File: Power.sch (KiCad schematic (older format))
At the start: 39 parts, among them J10 AUX, J8 MCU_CURRENT, J9 RAM_CURRENT, U1 ATXMEGA128A1U-AU, U4 SN74AHC573PW, U6 TPS2110A, U7 LM3671MF

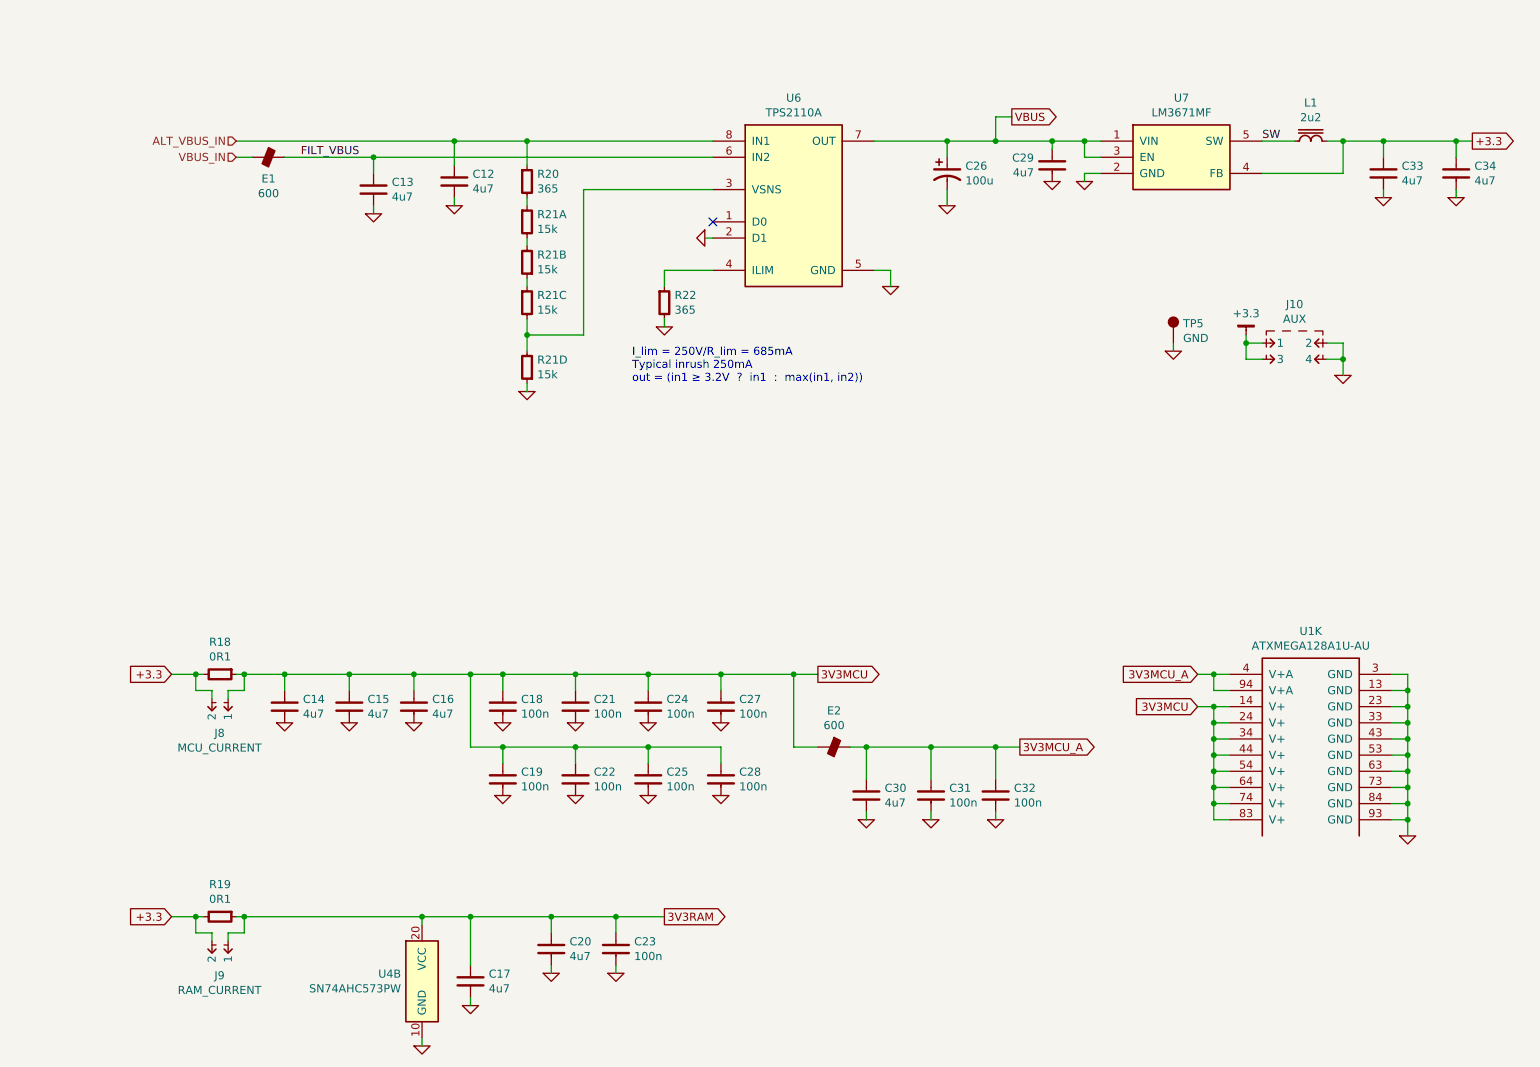
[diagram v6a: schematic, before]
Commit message: Remove extra resistor R20
With increase of R21 to 15k, it became insignificant - judged better
to remove it and push the power switching threshold a bit lower than
to add another BOM item to increase it.
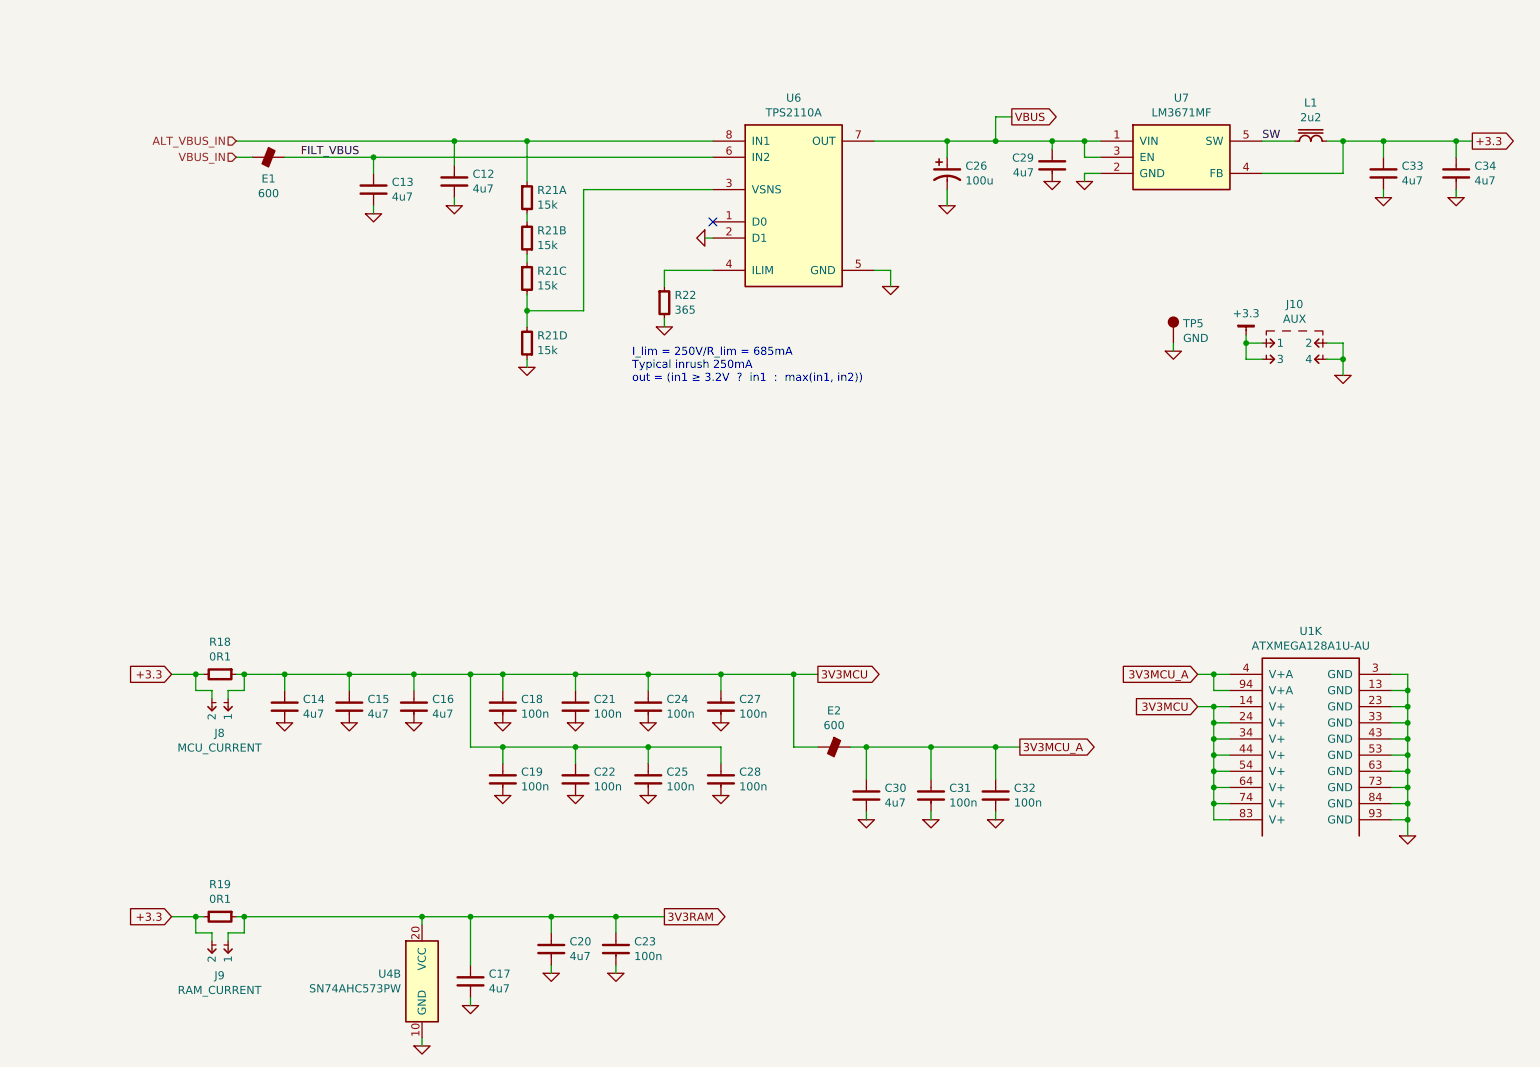
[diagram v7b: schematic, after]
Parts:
- removed R20: 365, IPC7351-Nominal:RESC1005X40, symbol R-0402
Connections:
- net ALT_VBUS_IN: now also R21.1
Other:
- moved on the sheet: R21A, R21B, R21C, R21D
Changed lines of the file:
@@
 L RESPACK-4X0603-CONV R?
 U 1 1 56F0A0E0
-P 3650 1900
+P 3650 1750
 AR Path="/56F0A0E0" Ref="R?"  Part="1"
 AR Path="/56EF633C/56F0A0E0" Ref="R21"  Part="1"
-F 0 "R21" H 3713 1946 50  0000 L CNN
-F 1 "15k" H 3713 1855 50  0000 L CNN
-F 2 "IPC7351-Nominal:RESCAXE80P160X320X70-8" H 3650 1900 50  0001 C CNN
-F 3 "" H 3650 1950 60  0000 C CNN
-F 4 "DIST DIGIKEY YC164J-15KCT-ND" H 3650 1900 60  0001 C CNN "BOM"
-	1    3650 1900
+F 0 "R21" H 3713 1796 50  0000 L CNN
+F 1 "15k" H 3713 1705 50  0000 L CNN
+F 2 "IPC7351-Nominal:RESCAXE80P160X320X70-8" H 3650 1750 50  0001 C CNN
+F 3 "" H 3650 1800 60  0000 C CNN
+F 4 "DIST DIGIKEY YC164J-15KCT-ND" H 3650 1750 60  0001 C CNN "BOM"
+	1    3650 1750
 	1    0    0    -1
 $EndComp
@@
 L RESPACK-4X0603-CONV R?
 U 2 1 56F0A2D7
-P 3650 2150
+P 3650 2000
 AR Path="/56F0A2D7" Ref="R?"  Part="1"
 AR Path="/56EF633C/56F0A2D7" Ref="R21"  Part="2"
-F 0 "R21" H 3587 2104 50  0000 R CNN
-F 1 "15k" H 3587 2195 50  0000 R CNN
-F 2 "IPC7351-Nominal:RESCAXE80P160X320X70-8" H 3650 2150 50  0001 C CNN
-F 3 "" H 3650 2200 60  0000 C CNN
-F 4 "DIST DIGIKEY YC164J-15KCT-ND" H 3650 2150 60  0001 C CNN "BOM"
-	2    3650 2150
+F 0 "R21" H 3587 1954 50  0000 R CNN
+F 1 "15k" H 3587 2045 50  0000 R CNN
+F 2 "IPC7351-Nominal:RESCAXE80P160X320X70-8" H 3650 2000 50  0001 C CNN
+F 3 "" H 3650 2050 60  0000 C CNN
+F 4 "DIST DIGIKEY YC164J-15KCT-ND" H 3650 2000 60  0001 C CNN "BOM"
+	2    3650 2000
 	-1   0    0    1
 $EndComp
@@
 L RESPACK-4X0603-CONV R?
 U 3 1 56F0A367
-P 3650 2400
+P 3650 2250
 AR Path="/56F0A367" Ref="R?"  Part="1"
 AR Path="/56EF633C/56F0A367" Ref="R21"  Part="3"
-F 0 "R21" H 3713 2446 50  0000 L CNN
-F 1 "15k" H 3713 2355 50  0000 L CNN
-F 2 "IPC7351-Nominal:RESCAXE80P160X320X70-8" H 3650 2400 50  0001 C CNN
-F 3 "" H 3650 2450 60  0000 C CNN
-F 4 "DIST DIGIKEY YC164J-15KCT-ND" H 3650 2400 60  0001 C CNN "BOM"
-	3    3650 2400
+F 0 "R21" H 3713 2296 50  0000 L CNN
+F 1 "15k" H 3713 2205 50  0000 L CNN
+F 2 "IPC7351-Nominal:RESCAXE80P160X320X70-8" H 3650 2250 50  0001 C CNN
+F 3 "" H 3650 2300 60  0000 C CNN
+F 4 "DIST DIGIKEY YC164J-15KCT-ND" H 3650 2250 60  0001 C CNN "BOM"
+	3    3650 2250
 	1    0    0    -1
 $EndComp
@@
 L RESPACK-4X0603-CONV R?
 U 4 1 56F0A408
-P 3650 2800
+P 3650 2650
 AR Path="/56F0A408" Ref="R?"  Part="1"
 AR Path="/56EF633C/56F0A408" Ref="R21"  Part="4"
-F 0 "R21" H 3587 2754 50  0000 R CNN
-F 1 "15k" H 3587 2845 50  0000 R CNN
-F 2 "IPC7351-Nominal:RESCAXE80P160X320X70-8" H 3650 2800 50  0001 C CNN
-F 3 "" H 3650 2850 60  0000 C CNN
-F 4 "DIST DIGIKEY YC164J-15KCT-ND" H 3650 2800 60  0001 C CNN "BOM"
-	4    3650 2800
+F 0 "R21" H 3587 2604 50  0000 R CNN
+F 1 "15k" H 3587 2695 50  0000 R CNN
+F 2 "IPC7351-Nominal:RESCAXE80P160X320X70-8" H 3650 2650 50  0001 C CNN
+F 3 "" H 3650 2700 60  0000 C CNN
+F 4 "DIST DIGIKEY YC164J-15KCT-ND" H 3650 2650 60  0001 C CNN "BOM"
+	4    3650 2650
 	-1   0    0    1
 $EndComp
@@
 L GND #PWR44
 U 1 1 56F0A481
-P 3650 2950
-F 0 "#PWR44" H 3650 2950 30  0001 C CNN
-F 1 "GND" H 3650 2880 30  0001 C CNN
-F 2 "" H 3650 2950 60  0000 C CNN
-F 3 "" H 3650 2950 60  0000 C CNN
-	1    3650 2950
+P 3650 2800
+F 0 "#PWR44" H 3650 2800 30  0001 C CNN
+F 1 "GND" H 3650 2730 30  0001 C CNN
+F 2 "" H 3650 2800 60  0000 C CNN
+F 3 "" H 3650 2800 60  0000 C CNN
+	1    3650 2800
 	1    0    0    -1
 $EndComp
@@
 Connection ~ 9100 5600
 Wire Wire Line
-	9100 4700 9100 5700
+	9100 4700 9100 4800
+Wire Wire Line
+	9100 4800 9100 4900
+Wire Wire Line
+	9100 4900 9100 5000
+Wire Wire Line
+	9100 5000 9100 5100
+Wire Wire Line
+	9100 5100 9100 5200
+Wire Wire Line
+	9100 5200 9100 5300
+Wire Wire Line
+	9100 5300 9100 5400
+Wire Wire Line
+	9100 5400 9100 5500
+Wire Wire Line
+	9100 5500 9100 5600
+Wire Wire Line
+	9100 5600 9100 5700
 Wire Wire Line
 	3000 6200 3000 6250
@@
 	3000 7000 3000 6950
 Wire Wire Line
-	5650 5150 6700 5150
+	5650 5150 5750 5150
+Wire Wire Line
+	5750 5150 6150 5150
+Wire Wire Line
+	6150 5150 6550 5150
+Wire Wire Line
+	6550 5150 6700 5150
 Wire Wire Line
 	6150 5150 6150 5350
@@
 	5750 5600 5750 5550
 Wire Wire Line
-	1850 4700 5450 4700
+	1850 4700 1900 4700
+Wire Wire Line
+	1900 4700 2150 4700
+Wire Wire Line
+	2150 4700 2550 4700
+Wire Wire Line
+	2550 4700 2950 4700
+Wire Wire Line
+	2950 4700 3300 4700
+Wire Wire Line
+	3300 4700 3500 4700
+Wire Wire Line
+	3500 4700 3950 4700
+Wire Wire Line
+	3950 4700 4400 4700
+Wire Wire Line
+	4400 4700 4850 4700
+Wire Wire Line
+	4850 4700 5300 4700
+Wire Wire Line
+	5300 4700 5450 4700
 Wire Wire Line
 	2150 4700 2150 4800
@@
 	5450 5150 5300 5150
 Wire Wire Line
-	1450 4700 1650 4700
+	1450 4700 1600 4700
+Wire Wire Line
+	1600 4700 1650 4700
 Connection ~ 2150 4700
 Wire Wire Line
@@
 	8200 2650 8100 2650
 Wire Wire Line
-	8100 2600 8100 2750
+	8100 2600 8100 2650
+Wire Wire Line
+	8100 2650 8100 2750
 Wire Wire Line
 	8100 2750 8200 2750
@@
 	9400 1400 9400 1500
 Wire Wire Line
-	8600 1400 9500 1400
-Wire Wire Line
-	8700 2650 8700 2850
+	8600 1400 8700 1400
+Wire Wire Line
+	8700 1400 8950 1400
+Wire Wire Line
+	8950 1400 9400 1400
+Wire Wire Line
+	9400 1400 9500 1400
+Wire Wire Line
+	8700 2650 8700 2750
+Wire Wire Line
+	8700 2750 8700 2850
 Wire Wire Line
 	8700 2650 8600 2650
@@
 	3300 4700 3300 5150
 Wire Wire Line
-	3300 5150 4850 5150
+	3300 5150 3500 5150
+Wire Wire Line
+	3500 5150 3950 5150
+Wire Wire Line
+	3950 5150 4400 5150
+Wire Wire Line
+	4400 5150 4850 5150
 Wire Wire Line
 	4850 5150 4850 5250
@@
 Connection ~ 5300 4700
 Wire Wire Line
-	7800 4700 8000 4700
+	7800 4700 7900 4700
+Wire Wire Line
+	7900 4700 8000 4700
 Wire Wire Line
 	7900 4700 7900 4800
@@
 Connection ~ 7900 4700
 Wire Wire Line
-	7800 4900 8000 4900
+	7800 4900 7900 4900
+Wire Wire Line
+	7900 4900 8000 4900
 Wire Wire Line
 	7900 5000 8000 5000
@@
 Connection ~ 7900 5500
 Wire Wire Line
-	7900 4900 7900 5600
+	7900 4900 7900 5000
+Wire Wire Line
+	7900 5000 7900 5100
+Wire Wire Line
+	7900 5100 7900 5200
+Wire Wire Line
+	7900 5200 7900 5300
+Wire Wire Line
+	7900 5300 7900 5400
+Wire Wire Line
+	7900 5400 7900 5500
+Wire Wire Line
+	7900 5500 7900 5600
 Wire Wire Line
 	3800 6200 3800 6300
@@
 	4200 6550 4200 6500
 Wire Wire Line
-	1850 6200 4500 6200
-Wire Wire Line
-	1450 6200 1650 6200
+	1850 6200 1900 6200
+Wire Wire Line
+	1900 6200 3000 6200
+Wire Wire Line
+	3000 6200 3300 6200
+Wire Wire Line
+	3300 6200 3800 6200
+Wire Wire Line
+	3800 6200 4200 6200
+Wire Wire Line
+	4200 6200 4500 6200
+Wire Wire Line
+	1450 6200 1600 6200
+Wire Wire Line
+	1600 6200 1650 6200
 Wire Wire Line
 	1700 6350 1700 6300
@@
 Connection ~ 3000 6200
 Wire Wire Line
-	5800 1400 7200 1400
-Wire Wire Line
-	1850 1400 4800 1400
+	5800 1400 6250 1400
+Wire Wire Line
+	6250 1400 6550 1400
+Wire Wire Line
+	6550 1400 6900 1400
+Wire Wire Line
+	6900 1400 7100 1400
+Wire Wire Line
+	7100 1400 7200 1400
+Wire Wire Line
+	1850 1400 3200 1400
+Wire Wire Line
+	3200 1400 3650 1400
+Wire Wire Line
+	3650 1400 4800 1400
 Wire Wire Line
 	4750 2000 4800 2000
@@
 	4500 2550 4500 2500
 Wire Wire Line
-	2150 1500 4800 1500
-Wire Wire Line
-	3650 1400 3650 1550
-Wire Wire Line
-	3650 2950 3650 2900
+	2150 1500 2700 1500
+Wire Wire Line
+	2700 1500 4800 1500
+Wire Wire Line
+	3650 2800 3650 2750
 Connection ~ 3650 1400
 Wire Wire Line
-	3650 2300 3650 2250
-Wire Wire Line
-	3650 2050 3650 2000
-Wire Wire Line
-	3650 2500 3650 2700
-Wire Wire Line
-	4000 1700 4000 2600
-Wire Wire Line
-	4000 2600 3650 2600
-Connection ~ 3650 2600
-Wire Wire Line
-	3650 1800 3650 1750
-$Comp
-L R-0402 R20
-U 1 1 56F0A8E6
-P 3650 1650
-F 0 "R20" H 3713 1696 50  0000 L CNN
-F 1 "365" H 3713 1605 50  0000 L CNN
-F 2 "IPC7351-Nominal:RESC1005X40" H 3650 1650 50  0001 C CNN
-F 3 "" H 3650 1700 60  0000 C CNN
-F 4 "RES SMD 365 1% [0402]" H 4400 2200 60  0001 C CNN "BOM"
-	1    3650 1650
-	1    0    0    -1
-$EndComp
+	3650 2150 3650 2100
+Wire Wire Line
+	3650 1900 3650 1850
+Wire Wire Line
+	3650 2350 3650 2450
+Wire Wire Line
+	3650 2450 3650 2550
+Wire Wire Line
+	4000 1700 4000 2450
+Wire Wire Line
+	4000 2450 3650 2450
+Connection ~ 3650 2450
+Wire Wire Line
+	3650 1650 3650 1400
 $Comp
 L C-0603 C?

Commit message: Decouple ALT_VBUS locally to U6
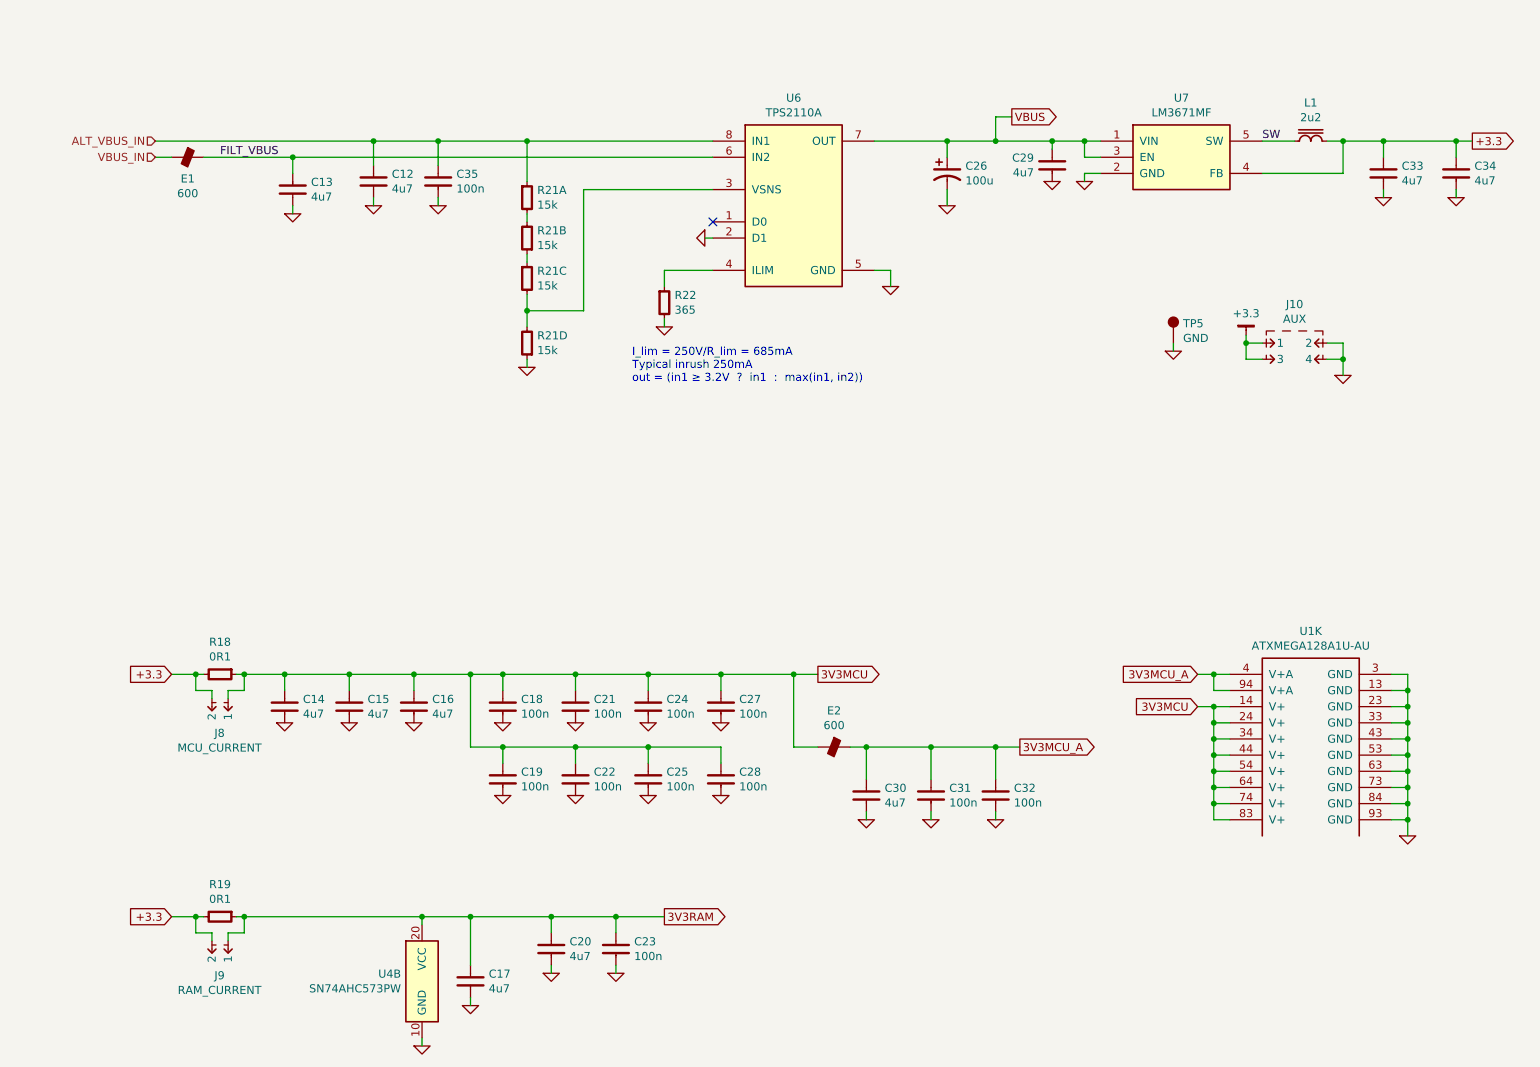
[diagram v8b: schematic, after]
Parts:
- added C35: 100n, IPC7351-Nominal:CAPC1005X55, symbol C-0402
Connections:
- net ALT_VBUS_IN: now also C35.1
- net GND: now also C35.2
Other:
- moved on the sheet: C12, C13, E1
